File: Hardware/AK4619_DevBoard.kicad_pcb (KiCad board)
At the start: 2 copper layers, 80 x 90 mm, 41 parts, among them J1 Out, J10 Conn_02x17_Odd_Even, J2 In, J7 Conn_02x10_Odd_Even, J8 Conn_02x08_Odd_Even, J9 Conn_02x15_Odd_Even, U2 AK4619VN

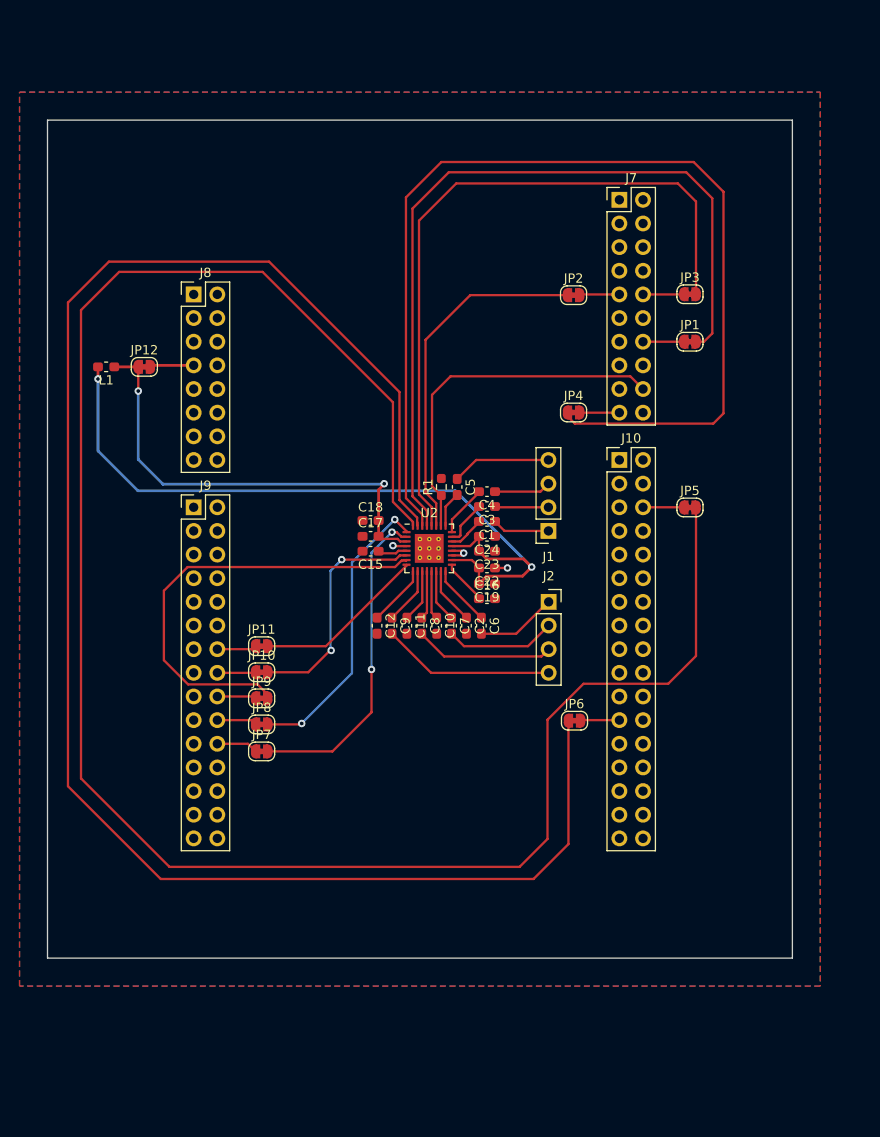
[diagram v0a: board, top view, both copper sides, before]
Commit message: Added HyperRam to Dev Board
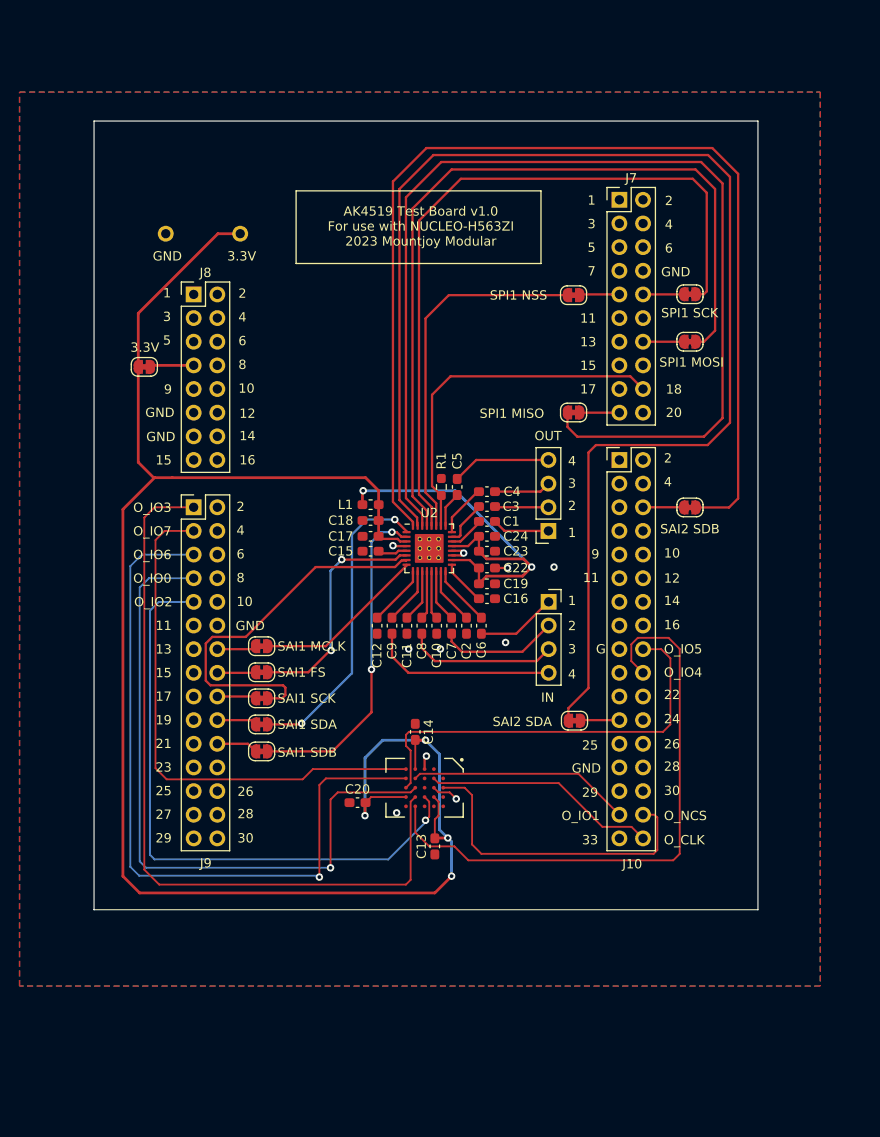
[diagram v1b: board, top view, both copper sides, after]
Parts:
- added C13: 100nF, Capacitor_SMD:C_0603_1608Metric_Pad1.08x0.95mm_HandSolder, F.Cu at (165.6, 105.0)
- added C14: 100nF, Capacitor_SMD:C_0603_1608Metric_Pad1.08x0.95mm_HandSolder, F.Cu at (163.5, 92.7)
- added C20: 100nF, Capacitor_SMD:C_0603_1608Metric_Pad1.08x0.95mm_HandSolder, F.Cu at (157.3, 100.3)
- added TP1: TestPoint, Custom_Footprints:1mm_Test_Point, F.Cu at (136.7, 39.2)
- added TP2: TestPoint, Custom_Footprints:1mm_Test_Point, F.Cu at (144.7, 39.2)
- added U1: Hyperram_BGA, Custom_Footprints:BGA-24_5x5_6.0x8.0mm, F.Cu at (164.5, 98.7)
- U2: footprint Package_DFN_QFN:QFN-32-1EP_5x5mm_P0.5mm_EP3.1x3.1mm_ThermalVias -> Custom_Footprints:QFN-32-1EP_5x5mm_P0.5mm_EP3.1x3.1mm_ThermalVias
- moved L1 32.0 mm to (158.7, 68.3)
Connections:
- net +3V3 renamed +3.3V
- J10 pad 15: unconnected-(J10-Pin_15-Pad15) -> /OCTOSPI_DQS
- J10 pad 18: unconnected-(J10-Pin_18-Pad18) -> /OCTOSPI_IO5
- J10 pad 20: unconnected-(J10-Pin_20-Pad20) -> /OCTOSPI_IO4
- J10 pad 31: unconnected-(J10-Pin_31-Pad31) -> /OCTOSPI_IO1
- J10 pad 32: unconnected-(J10-Pin_32-Pad32) -> /OCTOSPI_NCS
- J10 pad 34: unconnected-(J10-Pin_34-Pad34) -> /OCTOSPI_CLK
- J9 pad 1: unconnected-(J9-Pin_1-Pad1) -> /OCTOSPI_IO3
- J9 pad 3: unconnected-(J9-Pin_3-Pad3) -> /OCTOSPI_IO7
- J9 pad 5: unconnected-(J9-Pin_5-Pad5) -> /OCTOSPI_IO6
- J9 pad 7: unconnected-(J9-Pin_7-Pad7) -> /OCTOSPI_IO0
- J9 pad 9: unconnected-(J9-Pin_9-Pad9) -> /OCTOSPI_IO2
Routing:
- net +3.3V: track 49.2 -> 192.6 mm, vias 2 -> 4
- net /SAI2_SD_B: track 208.3 -> 117.3 mm
- net /OCTOSPI_IO3: track 0.00 -> 82.2 mm
- net /OCTOSPI_IO6: track 0.00 -> 79.9 mm, vias 0 -> 1
- net /OCTOSPI_IO0: track 0.00 -> 73.4 mm, vias 0 -> 1
- net /OCTOSPI_IO2: track 0.00 -> 65.8 mm, vias 0 -> 1
- net /OCTOSPI_IO4: track 0.00 -> 64.3 mm
- net /OCTOSPI_IO7: track 0.00 -> 56.9 mm
- net /OCTOSPI_IO5: track 0.00 -> 45.4 mm
- net +3.3VA: track 83.2 -> 45.8 mm
- net /SAI2_SD_A: track 183.0 -> 147.6 mm
- net /OCTOSPI_NCS: track 0.00 -> 34.4 mm
- net /OCTOSPI_CLK: track 0.00 -> 25.1 mm
- net /OCTOSPI_IO1: track 0.00 -> 23.9 mm
- net /SAI1_SCK_A: track 48.0 -> 41.0 mm
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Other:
- board size 80 x 90 mm -> 71.3 x 84.7 mm
- board text added: "1"
- board text added: "10"
- board text added: "11"
- board text added: "12"
- board text added: "13"
- board text added: "14"
- board text added: "15"
- board text added: "16"
- board text added: "17"
- board text added: "18"
- board text added: "19"
- board text added: "2"
- board text added: "20"
- board text added: "21"
- board text added: "22"
- board text added: "23"
- board text added: "24"
- board text added: "25"
- board text added: "26"
- board text added: "27"
- board text added: "28"
- board text added: "29"
- board text added: "3"
- board text added: "3.3V"
- board text added: "30"
- board text added: "33"
- board text added: "4"
- board text added: "5"
- board text added: "6"
- board text added: "7"
- board text added: "8"
- board text added: "9"
- board text added: "AK4519 Test Board v1.0 For use with NUCLEO-H563ZI 2023 Mountjoy Modular"
- board text added: "G"
- board text added: "GND"
- board text added: "IN"
- board text added: "OUT"
- board text added: "O_CLK"
- board text added: "O_IO0"
- board text added: "O_IO1"
- board text added: "O_IO2"
- board text added: "O_IO3"
- board text added: "O_IO4"
- board text added: "O_IO5"
- board text added: "O_IO6"
- board text added: "O_IO7"
- board text added: "O_NCS"
- board text added: "SAI1 FS"
- board text added: "SAI1 MCLK"
- board text added: "SAI1 SCK"
- board text added: "SAI1 SDA"
- board text added: "SAI1 SDB"
- board text added: "SAI2 SDA"
- board text added: "SAI2 SDB"
- board text added: "SPI1 MISO"
- board text added: "SPI1 MOSI"
- board text added: "SPI1 NSS"
- board text added: "SPI1 SCK"

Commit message: Added Input scaling
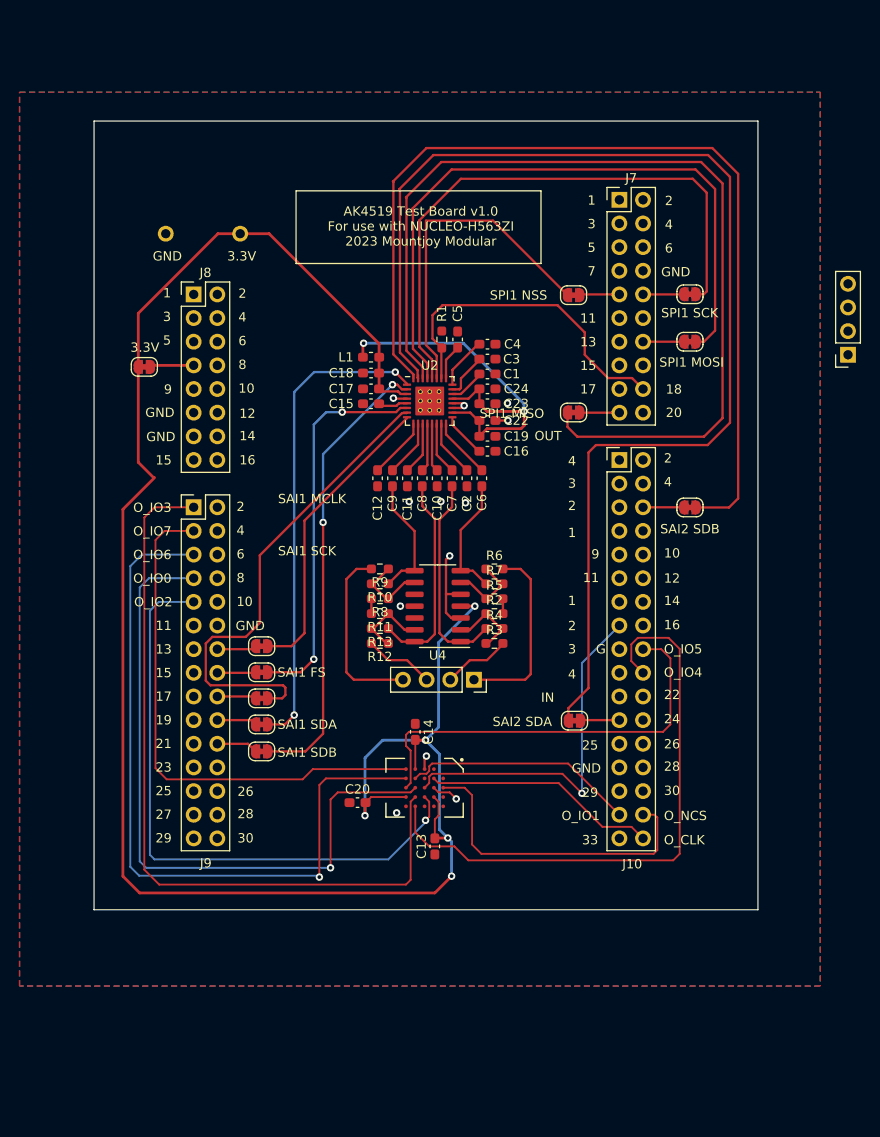
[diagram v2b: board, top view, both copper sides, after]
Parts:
- added R10: 14k, Resistor_SMD:R_0603_1608Metric_Pad0.98x0.95mm_HandSolder, F.Cu at (159.7, 76.8)
- added R11: 100k, Resistor_SMD:R_0603_1608Metric_Pad0.98x0.95mm_HandSolder, F.Cu at (159.7, 80.0)
- added R12: 68k, Resistor_SMD:R_0603_1608Metric_Pad0.98x0.95mm_HandSolder, F.Cu at (159.7, 83.2)
- added R13: 14k, Resistor_SMD:R_0603_1608Metric_Pad0.98x0.95mm_HandSolder, F.Cu at (159.7, 81.6)
- added R2: 100k, Resistor_SMD:R_0603_1608Metric_Pad0.98x0.95mm_HandSolder, F.Cu at (172.0, 80.0)
- added R3: 68k, Resistor_SMD:R_0603_1608Metric_Pad0.98x0.95mm_HandSolder, F.Cu at (172.0, 83.2)
- added R4: 14k, Resistor_SMD:R_0603_1608Metric_Pad0.98x0.95mm_HandSolder, F.Cu at (172.0, 81.6)
- added R5: 100k, Resistor_SMD:R_0603_1608Metric_Pad0.98x0.95mm_HandSolder, F.Cu at (172.0, 78.4)
- added R6: 68k, Resistor_SMD:R_0603_1608Metric_Pad0.98x0.95mm_HandSolder, F.Cu at (172.0, 75.2)
- added R7: 14k, Resistor_SMD:R_0603_1608Metric_Pad0.98x0.95mm_HandSolder, F.Cu at (172.0, 76.8)
- added R8: 100k, Resistor_SMD:R_0603_1608Metric_Pad0.98x0.95mm_HandSolder, F.Cu at (159.7, 78.4)
- added R9: 68k, Resistor_SMD:R_0603_1608Metric_Pad0.98x0.95mm_HandSolder, F.Cu at (159.7, 75.2)
- added U4: MCP6004, Package_SO:SO-14_3.9x8.65mm_P1.27mm, F.Cu at (165.9, 79.2)
- moved J1 37.3 mm to (210.0, 52.2)
- moved C16 15.8 mm to (171.2, 62.6)
- moved C17 15.8 mm to (158.8, 55.9)
- moved C24 15.8 mm to (171.2, 55.9)
- moved C4 15.8 mm to (171.2, 51.1)
- moved C5 15.8 mm to (168.1, 50.6)
- moved R1 15.8 mm to (166.3, 50.6)
- moved C15 15.8 mm to (158.8, 57.5)
- moved C18 15.8 mm to (158.8, 54.2)
- moved C19 15.8 mm to (171.2, 61.0)
- moved C23 15.8 mm to (171.2, 57.5)
- moved C3 15.8 mm to (171.2, 52.7)
- moved L1 15.8 mm to (158.8, 52.5)
- moved U2 15.8 mm to (165.1, 57.2)
- moved C1 15.8 mm to (171.2, 54.3)
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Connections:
- C6 pad 2: /IN1 -> /Audio_In1
- C7 pad 2: /IN2 -> /Audio_In2
- C8 pad 2: /IN3 -> /Audio_In3
- C9 pad 2: /IN4 -> /Audio_In4
- U1 pad C3: unconnected-(U1-RWDS-PadC3) -> /OCTOSPI_DQS
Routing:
- net /OCTOSPI_DQS: track 0.00 -> 38.5 mm, vias 0 -> 1
- net /Audio_In3: track 0.00 -> 22.3 mm
- net /Audio_In2: track 0.00 -> 22.3 mm
- net /SAI1_SD_A: track 33.4 -> 51.6 mm
- net /SAI1_FS_A: track 25.2 -> 41.5 mm
- net /SPI1_MOSI: track 87.6 -> 71.7 mm
- net /SPI1_MISO: track 117.2 -> 101.4 mm
- net /SAI2_SD_B: track 117.3 -> 101.5 mm
- net /SAI2_SD_A: track 147.6 -> 131.8 mm
- net /SPI1_SCK: track 78.6 -> 62.8 mm
- net /SAI1_MCLK_A: track 18.6 -> 32.3 mm
- net /SAI1_SD_B: track 35.6 -> 49.1 mm
- net /Audio_In4: track 0.00 -> 13.4 mm
- net /Audio_In1: track 0.00 -> 13.3 mm
- net +3.3V: track 192.6 -> 205.8 mm, vias 4 -> 5
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
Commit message: Added Ouput op-amp
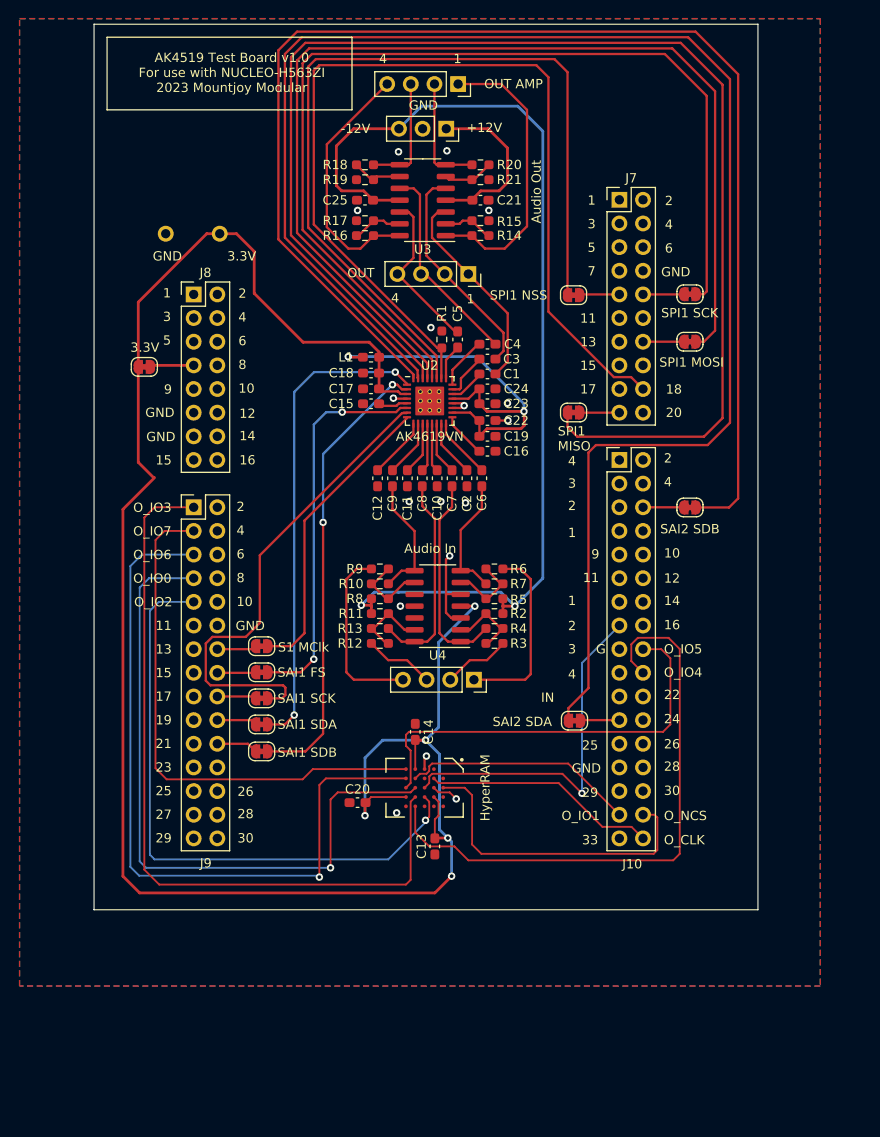
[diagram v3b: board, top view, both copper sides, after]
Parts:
- added C21: 100nF, Capacitor_SMD:C_0603_1608Metric_Pad1.08x0.95mm_HandSolder, F.Cu at (170.5, 35.6)
- added C25: 100nF, Capacitor_SMD:C_0603_1608Metric_Pad1.08x0.95mm_HandSolder, F.Cu at (158.1, 35.6)
- added J3: Out, Connector_PinSocket_2.54mm:PinSocket_1x03_P2.54mm_Vertical, F.Cu at (166.8, 27.9)
- added J4: Out, Connector_PinSocket_2.54mm:PinSocket_1x04_P2.54mm_Vertical, F.Cu at (168.1, 23.1)
- added R14: 14k, Resistor_SMD:R_0603_1608Metric_Pad0.98x0.95mm_HandSolder, F.Cu at (170.5, 39.4)
- added R15: 10k, Resistor_SMD:R_0603_1608Metric_Pad0.98x0.95mm_HandSolder, F.Cu at (170.5, 37.8)
- added R16: 14k, Resistor_SMD:R_0603_1608Metric_Pad0.98x0.95mm_HandSolder, F.Cu at (158.1, 39.4)
- added R17: 10k, Resistor_SMD:R_0603_1608Metric_Pad0.98x0.95mm_HandSolder, F.Cu at (158.1, 37.8)
- added R18: 14k, Resistor_SMD:R_0603_1608Metric_Pad0.98x0.95mm_HandSolder, F.Cu at (158.1, 31.8)
- added R19: 10k, Resistor_SMD:R_0603_1608Metric_Pad0.98x0.95mm_HandSolder, F.Cu at (158.1, 33.4)
- added R20: 14k, Resistor_SMD:R_0603_1608Metric_Pad0.98x0.95mm_HandSolder, F.Cu at (170.5, 31.8)
- added R21: 10k, Resistor_SMD:R_0603_1608Metric_Pad0.98x0.95mm_HandSolder, F.Cu at (170.5, 33.4)
- added U3: TL074, Package_SO:SO-14_3.9x8.65mm_P1.27mm, F.Cu at (164.3, 35.6)
- moved J1 41.7 mm to (169.2, 43.5), turned to -90 degrees
- moved TP2 2.20 mm to (142.5, 39.2)
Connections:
- net /-12V renamed -12V
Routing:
- net -12V: track 3.20 -> 112.3 mm, vias 0 -> 2
- net /PDN: track 35.4 -> 103.8 mm
- net /SPI1_NSS: track 35.9 -> 91.9 mm
- net /SPI1_SCK: track 62.8 -> 107.5 mm
- net /SPI1_MOSI: track 71.7 -> 115.5 mm
- net /SPI1_MISO: track 101.4 -> 144.5 mm
- net /SAI2_SD_A: track 131.8 -> 174.3 mm
- net /SAI2_SD_B: track 101.5 -> 143.8 mm
- net /OUT_AMP1: track 0.00 -> 31.4 mm
- net /OUT_AMP4: track 0.00 -> 27.4 mm
- net /OUT2: track 0.00 -> 23.8 mm
- net /OUT1: track 0.00 -> 22.4 mm
- net /OUT3: track 0.00 -> 22.1 mm
- net +12V: track 0.00 -> 18.5 mm
- net /OUT4: track 0.00 -> 17.6 mm
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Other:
- board size 71.3 x 84.7 mm -> 71.3 x 95.1 mm
- board text added: "+12V"
- board text added: "-12V"
- board text added: "Audio In"
- board text added: "Audio Out"
- board text added: "HyperRAM"
- board text added: "OUT AMP"
- board text added: "S1 MClk"
- board text removed: "SAI1 MCLK"

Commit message: DevBoard Gerbers ordered
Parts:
- added J2: Power, Connector_PinSocket_2.54mm:PinSocket_1x02_P2.54mm_Vertical, F.Cu at (138.9, 47.8)
- J1: renamed from J3; value Out -> Power
- J5: renamed from J4; value Out -> Out_Amp
- moved JP7 27.0 mm to (180.5, 72.8)
- moved J3 17.3 mm to (169.8, 104.4)
- moved JP12 17.3 mm to (193.0, 85.9)
- moved JP4 17.3 mm to (147.0, 106.4)
- moved R10 17.3 mm to (172.0, 98.9)
- moved R13 17.3 mm to (159.7, 98.9)
- moved C15 17.3 mm to (158.8, 71.5)
- moved C19 17.3 mm to (171.2, 78.3)
- moved C21 17.3 mm to (171.2, 70.0)
- moved C24 17.3 mm to (158.8, 74.8)
- moved C4 17.3 mm to (171.2, 74.8)
- moved J4 17.3 mm to (169.2, 60.8)
- moved J6 17.3 mm to (139.7, 63.0)
- moved JP8 17.3 mm to (180.5, 75.7)
- moved L1 17.3 mm to (158.8, 69.8)
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- renumbered C21 to C1, C7 to C10, C8 to C11, C9 to C12, C20 to C13, C18 to C15, C13 to C16, C22 to C18, C25 to C2, C1 to C20, C3 to C21, C4 to C22, C5 to C23, C15 to C24, C16 to C25, C24 to C3, C23 to C4, C2 to C5, C10 to C6, C11 to C7, C12 to C8, C6 to C9, J2 to J3, J1 to J4, J8 to J6, J9 to J7, J7 to J8, J10 to J9, JP12 to JP1, JP3 to JP10, JP1 to JP11, JP5 to JP12, JP11 to JP2, JP10 to JP3, JP9 to JP4, JP8 to JP5, JP7 to JP6, JP2 to JP7, JP4 to JP8, JP6 to JP9, R4 to R10, R7 to R11, R10 to R12, R19 to R14, R17 to R15, R15 to R16, R21 to R17, R16 to R19, R14 to R20, R20 to R21, R5 to R4, R6 to R5, R8 to R6, R9 to R7, R11 to R8, R12 to R9, U3 to U1, U4 to U2, U1 to U3, U2 to U4
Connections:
- J8 pad 17: unconnected-(J7-Pin_17-Pad17) (its old number) -> Net-(J8-Pin_17)
- J8 pad 9: Net-(J7-Pin_9) -> unconnected-(J8-Pin_9-Pad9)
- JP7 pad 2: Net-(J7-Pin_9) -> Net-(J8-Pin_17)
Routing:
- net +12V: track 18.5 -> 50.0 mm
- net -12V: track 112.3 -> 134.9 mm
- net /SPI1_NSS: track 91.9 -> 101.6 mm
- net /PDN: track 103.8 -> 109.6 mm
- net Net-(J8-Pin_17): track 0.00 -> 4.43 mm
- net Net-(J7-Pin_9): track 4.30 -> 0.00 mm
- net +3.3V: track 208.6 -> 204.6 mm
- net GND: vias 17 -> 144
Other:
- board size 71.3 x 95.1 mm -> 72.4 x 98 mm
